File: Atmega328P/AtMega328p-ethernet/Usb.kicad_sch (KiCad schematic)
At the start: 4 parts, among them J2 USB_C_Receptacle_USB2.0_16P, U3 MCP2200-I-SS

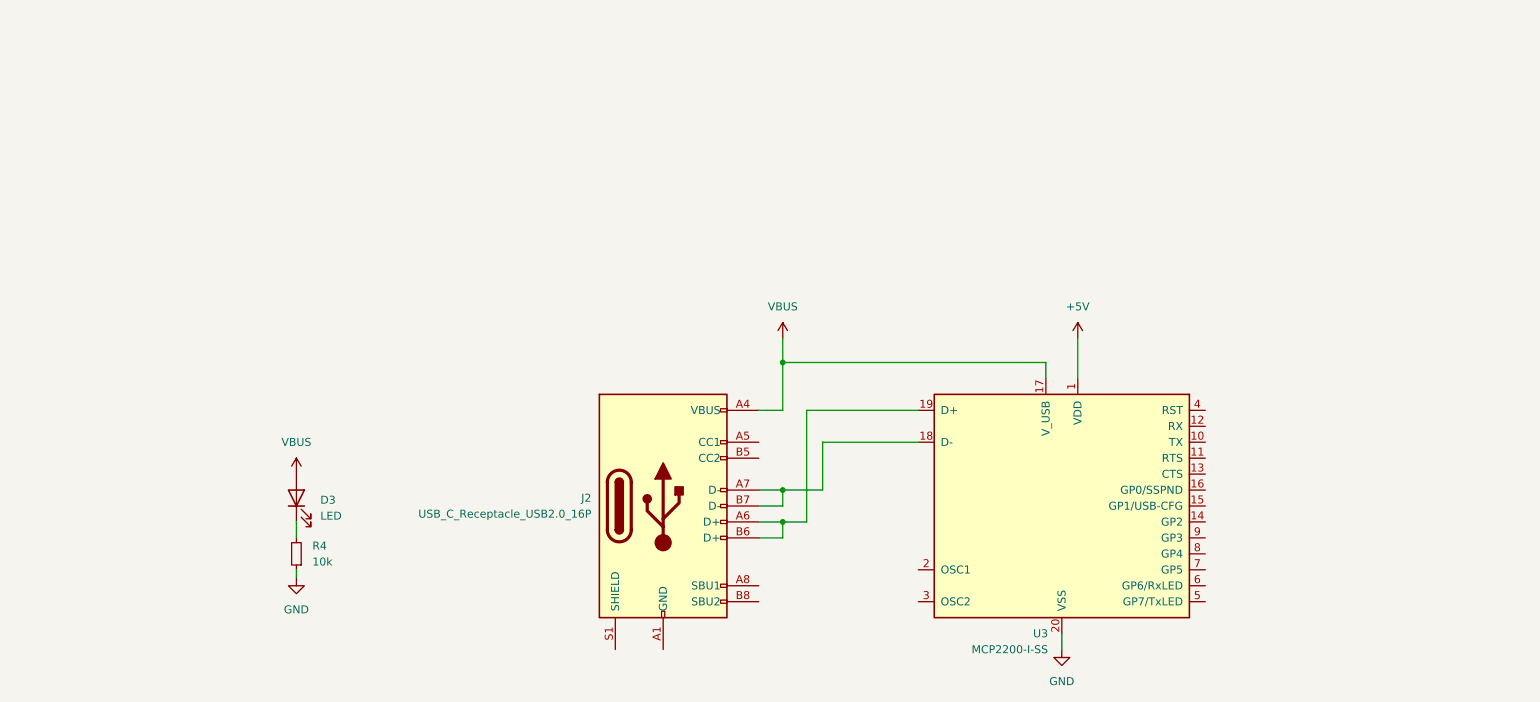
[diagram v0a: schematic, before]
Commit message: Most main components layed out
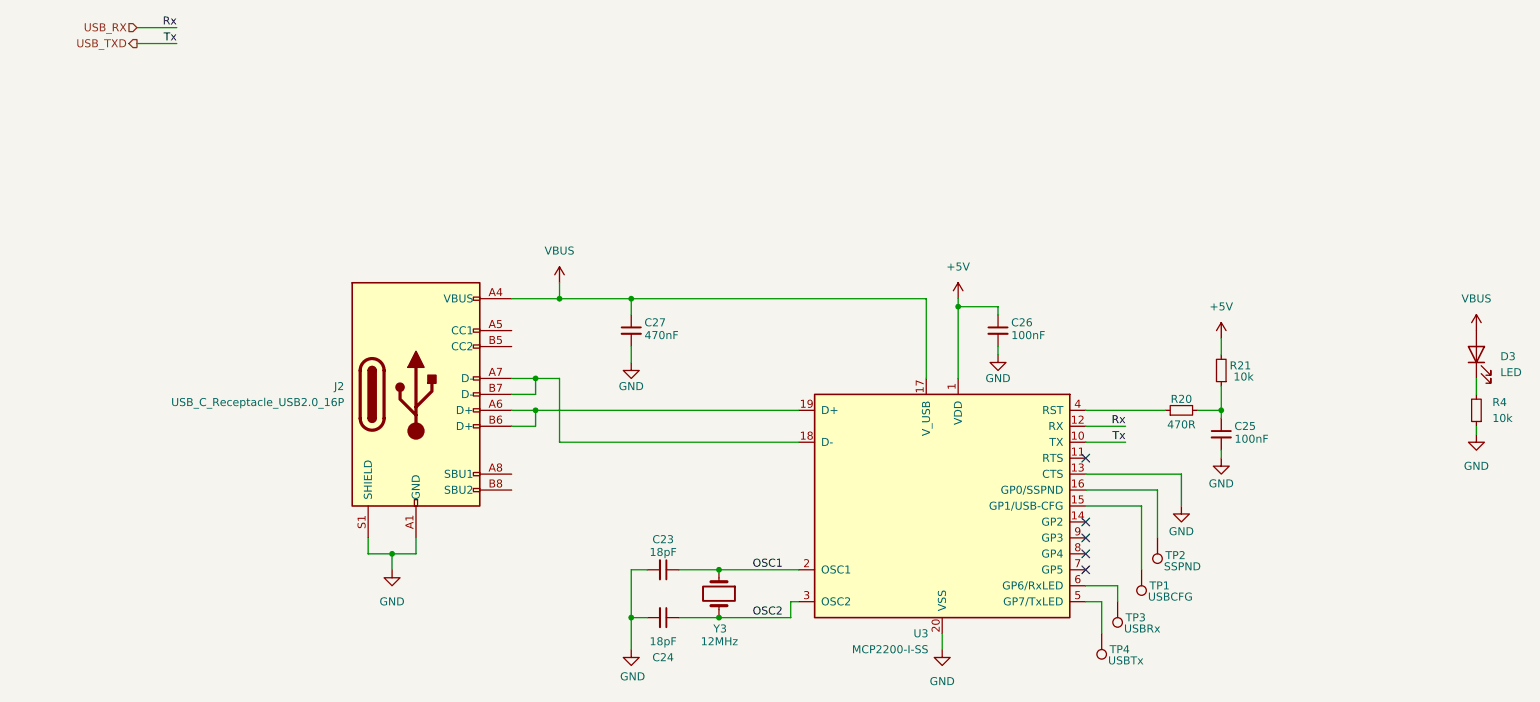
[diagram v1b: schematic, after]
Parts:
- added C23, C24: 18pF, symbol Device:C_Small
- added C25, C26: 100nF, symbol Device:C_Small
- added C27: 470nF, symbol Device:C_Small
- added R20: 470R, symbol Device:R_Small
- added R21: 10k, symbol Device:R_Small
- added TP1: USBCFG, symbol Connector:TestPoint
- added TP2: SSPND, symbol Connector:TestPoint
- added TP3: USBRx, symbol Connector:TestPoint
- added TP4: USBTx, symbol Connector:TestPoint
- added Y3: 12MHz, symbol Device:Crystal
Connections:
- net +5V: now also C26.1, R21.2
- net GND: now also J2.A1 (GND), J2.A12 (GND), J2.B1 (GND), J2.B12 (GND), J2.S1 (SHIELD), U3.13 (CTS), C23.2, C24.2, C25.2, C26.2, C27.2
- net VBUS: now also C27.1
- net USB_TXD: now reaches U3.10 (TX)
- net USB_RX: now reaches U3.12 (RX)
- net at U3.15 (GP1/USB-CFG): now also TP1.1
- net at U3.16 (GP0/SSPND): now also TP2.1
- net OSC1: now reaches U3.2 (OSC1)
- net OSC1: now also C23.1, Y3.1
- net OSC2: now reaches U3.3 (OSC2)
- net OSC2: now also C24.1, Y3.2
- net at U3.4 (RST): now also R20.1
- net at U3.5 (GP7/TxLED): now also TP4.1
- net at U3.6 (GP6/RxLED): now also TP3.1
- new net: C25.1, R20.2, R21.1
- no-connect marks 0 -> 5
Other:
- moved on the sheet: D3, J2, R4, U3

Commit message: Schematic draft complete
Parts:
- added FB2: HH-1M1608-121JT, Inductor_SMD:L_0603_1608Metric, symbol Device:FerriteBead_Small
- C23, C24, C25, C26, C27: footprint (none) -> Capacitor_SMD:C_0603_1608Metric
- D3: footprint (none) -> LED_SMD:LED_0603_1608Metric
- J2: footprint (none) -> Connector_USB:USB_C_Receptacle_Amphenol_124019772112A
- R20, R21, R4: footprint (none) -> Resistor_SMD:R_0603_1608Metric
- TP1, TP2, TP3, TP4: footprint (none) -> TestPoint:TestPoint_Pad_D4.0mm
- Y3: footprint (none) -> Crystal:Crystal_SMD_2012-2Pin_2.0x1.2mm
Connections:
- net +5V: now also FB2.2
- net VBUS: now also FB2.1
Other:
- company: (none) -> HUNTER INC.
- title: (none) -> USB INTERFACE
- moved on the sheet: C26, C27, D3, J2, R4

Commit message: PCB Layout done initial
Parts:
- TP1, TP2, TP3, TP4: footprint TestPoint:TestPoint_Pad_D4.0mm -> TestPoint:TestPoint_Pad_1.0x1.0mm
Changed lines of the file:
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@@
 			)
 		)
-		(property "Footprint" "TestPoint:TestPoint_Pad_D4.0mm"
+		(property "Footprint" "TestPoint:TestPoint_Pad_1.0x1.0mm"
 			(at 189.23 116.84 0)
 			(effects
@@
 			)
 		)
-		(property "Footprint" "TestPoint:TestPoint_Pad_D4.0mm"
+		(property "Footprint" "TestPoint:TestPoint_Pad_1.0x1.0mm"
 			(at 195.58 106.68 0)
 			(effects
@@
 			)
 		)
-		(property "Footprint" "TestPoint:TestPoint_Pad_D4.0mm"
+		(property "Footprint" "TestPoint:TestPoint_Pad_1.0x1.0mm"
 			(at 186.69 121.92 0)
 			(effects
@@
 			)
 		)
-		(property "Footprint" "TestPoint:TestPoint_Pad_D4.0mm"
+		(property "Footprint" "TestPoint:TestPoint_Pad_1.0x1.0mm"
 			(at 193.04 111.76 0)
 			(effects

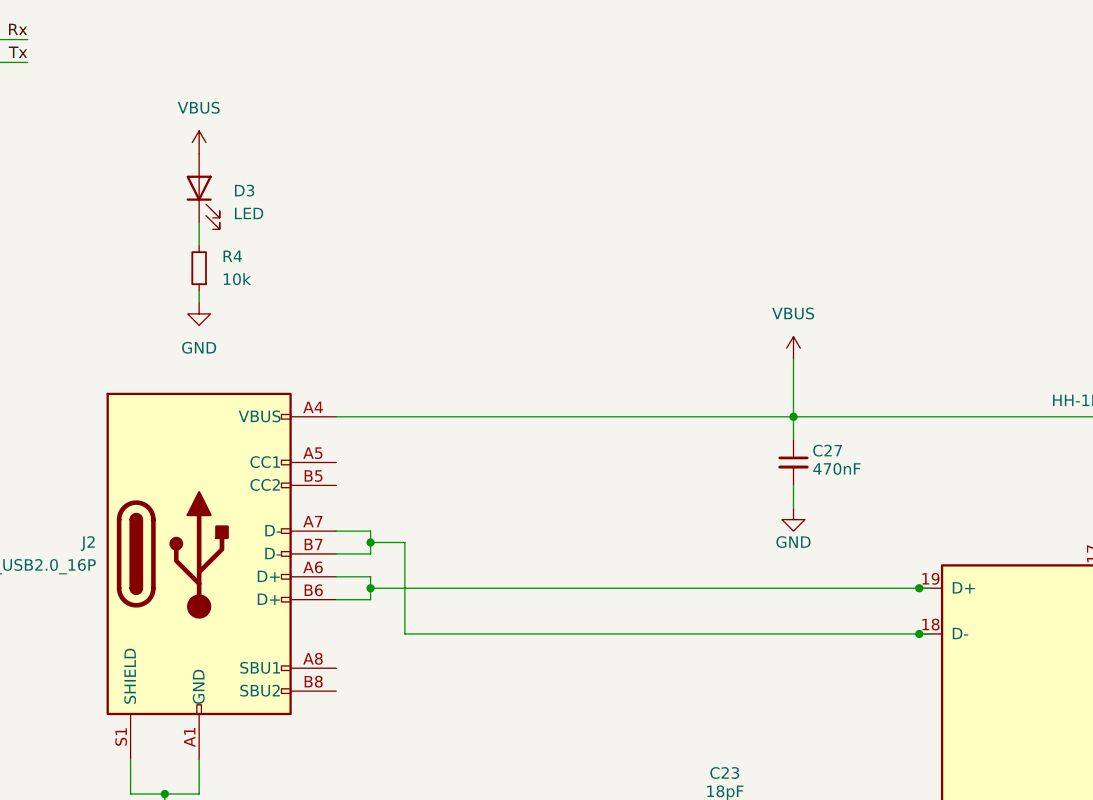
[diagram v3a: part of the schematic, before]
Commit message: Added dif pair and finished USB schematic
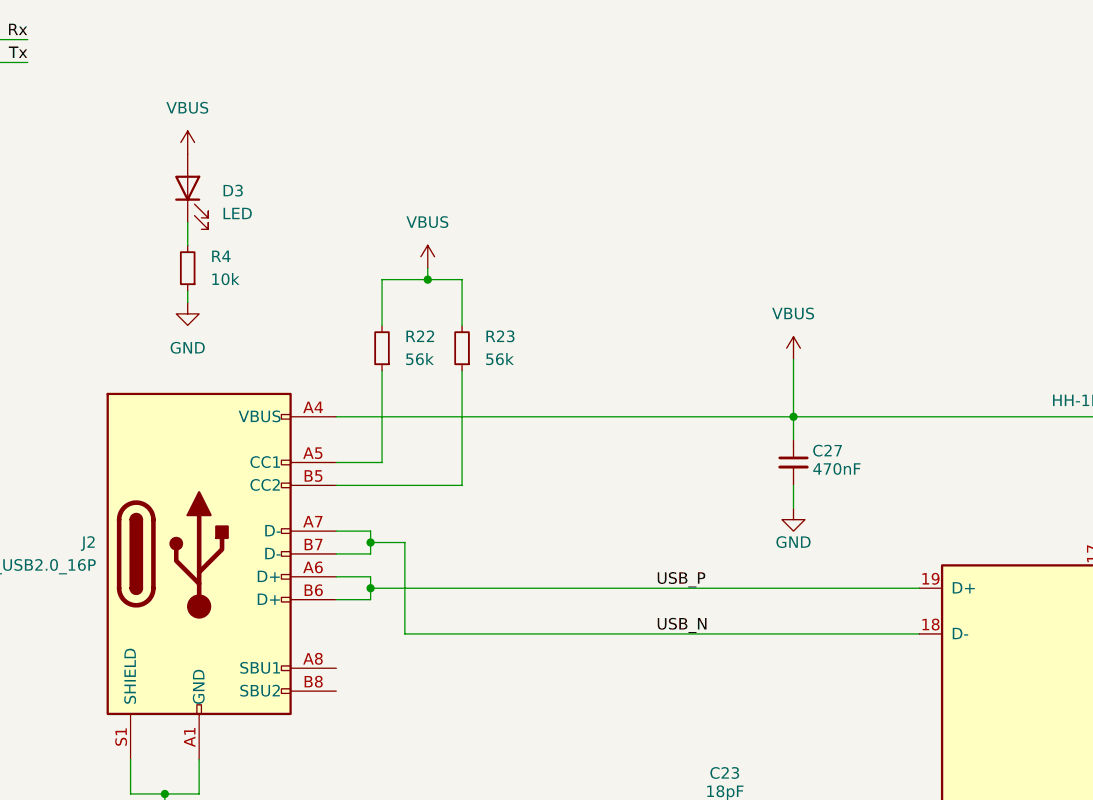
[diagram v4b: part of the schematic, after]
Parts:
- added R22, R23: 56k, Resistor_SMD:R_0603_1608Metric, symbol Device:R_Small
- J2: footprint Connector_USB:USB_C_Receptacle_Amphenol_124019772112A -> Connector_USB:USB_C_Receptacle_G-Switch_GT-USB-7010ASV
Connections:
- net VBUS: now also R22.2, R23.2
- net USB_N: now reaches J2.A7 (D-), J2.B7 (D-), U3.18 (D-)
- net USB_P: now reaches J2.A6 (D+), J2.B6 (D+), U3.19 (D+)
- net at J2.A5 (CC1): now also R22.1
- net at J2.B5 (CC2): now also R23.1
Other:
- moved on the sheet: D3, R4
